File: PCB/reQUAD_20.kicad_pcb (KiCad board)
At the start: 2 copper layers, 51.3 x 18.3 mm, 12 parts, among them J1 Model_100_System_BUS, U1 AS6C1008, U2 74x573, U3 74x2G79, U4 74x02

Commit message: datasheets
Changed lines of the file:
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@@
     (fp_arc (start 4.905239 -2.551328) (mid 4.8 -2.952056) (end 4.906989 -3.352321)
       (stroke (width 0.1) (type default)) (layer "B.SilkS"))
-    (fp_arc (start 5.224755 -1.996844) (mid 5.280901 -1.852056) (end 5.3 -1.697943)
+    (fp_arc (start 5.224755 -1.996844) (mid 5.280886 -1.852055) (end 5.3 -1.697943)
       (stroke (width 0.1) (type default)) (layer "B.SilkS"))
     (fp_line (start -6.35 -1.6375) (end -6.35 1.6375)
@@
   (via (at 170.32 100) (size 0.5) (drill 0.3) (layers "F.Cu" "B.Cu") (net 1))
   (via (at 160 98.35) (size 0.5) (drill 0.3) (layers "F.Cu" "B.Cu") (free) (net 1))
-  (via (at 125.925 98.45) (size 0.5) (drill 0.3) (layers "F.Cu" "B.Cu") (free) (net 1))
+  (via (at 125.8 99.45) (size 0.5) (drill 0.3) (layers "F.Cu" "B.Cu") (free) (net 1))
   (via (at 172.86 106.096) (size 0.5) (drill 0.3) (layers "F.Cu" "B.Cu") (free) (net 1))
   (via (at 166.51 95.809) (size 0.5) (drill 0.3) (layers "F.Cu" "B.Cu") (free) (net 1))

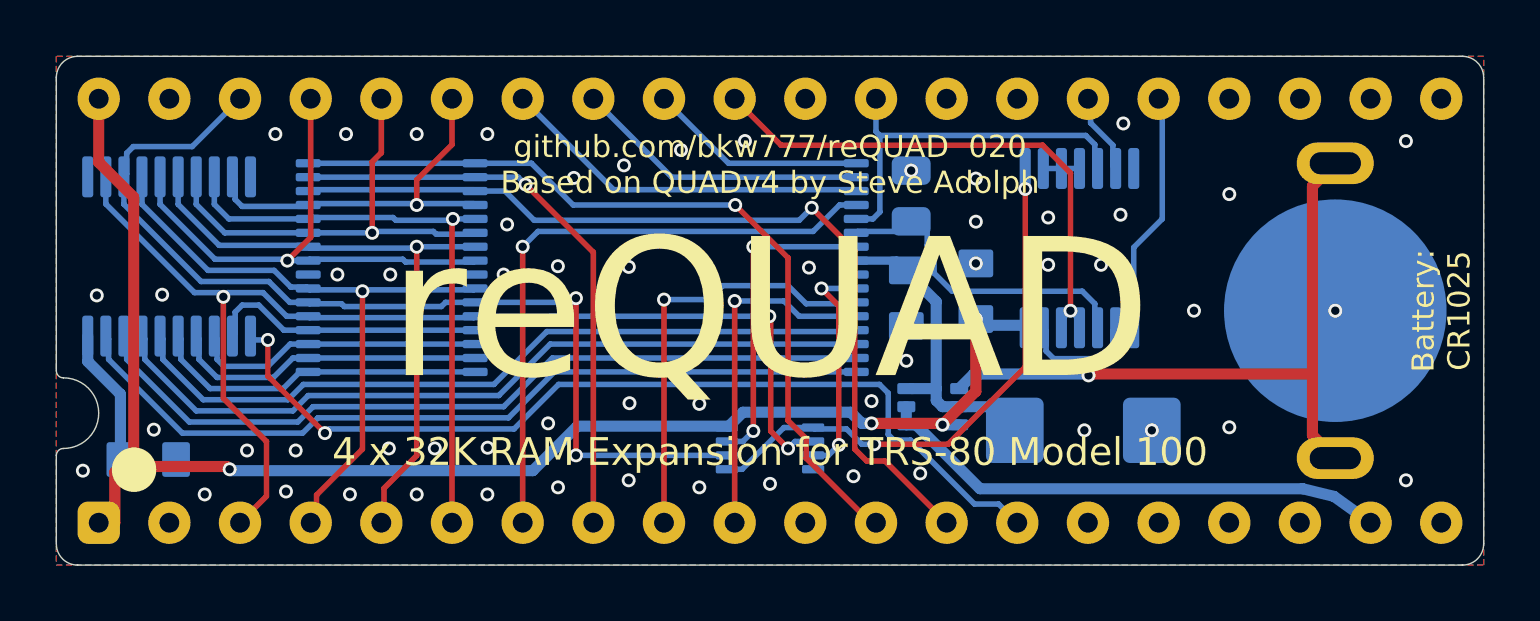
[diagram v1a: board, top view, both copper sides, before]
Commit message: tiny pcb layout nudges
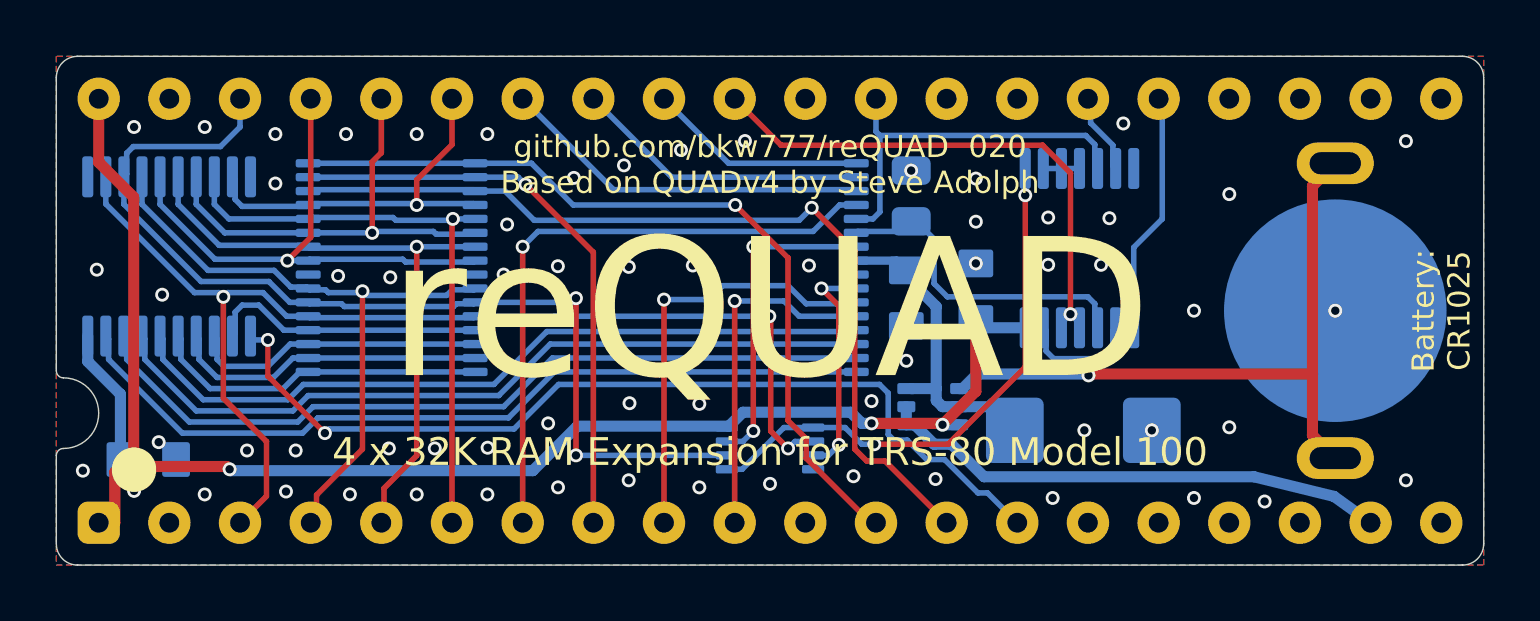
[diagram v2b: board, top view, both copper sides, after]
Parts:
- C1, C2, C3: value 0.1u -> 1u
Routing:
- net /AD1: track 35.7 -> 36.3 mm
- net GND: vias 59 -> 66
